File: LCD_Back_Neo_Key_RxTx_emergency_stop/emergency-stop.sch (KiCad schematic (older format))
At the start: 11 parts, among them J6 Screw_Terminal_01x05, K1 FINDER-34.51, K2 FINDER-34.51, K3 FINDER-34.51, Q2 2N2222

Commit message: combine screw terminal
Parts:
- removed J6: Screw_Terminal_01x05, TerminalBlock:TerminalBlock_bornier-5_P5.08mm, symbol Connector:Screw_Terminal_01x05
- removed S1: Emergency Button, symbol LCD_Back_Neo_Key_RxTx_emergency_stop-rescue:Ext_switch
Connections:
- net labels added: ScrewTerm10-EmrgencyRelay12, ScrewTerm11-EmrgencyRelay14, ScrewTerm12-EmrgencyRelay11, ScrewTerm13-EmergencyStopSwitch1, ScrewTerm14-EmergencyStopSwitch2
- wire segments 58 -> 52
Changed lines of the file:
@@
 Wire Wire Line
 	4300 4750 4300 5550
-$Comp
-L Connector:Screw_Terminal_01x05 J6
-U 1 1 5CEE591F
-P 8250 5500
-F 0 "J6" H 8330 5542 50  0000 L CNN
-F 1 "Screw_Terminal_01x05" H 8330 5451 50  0000 L CNN
-F 2 "TerminalBlock:TerminalBlock_bornier-5_P5.08mm" H 8250 5500 50  0001 C CNN
-F 3 "~" H 8250 5500 50  0001 C CNN
-	1    8250 5500
-	1    0    0    -1
-$EndComp
 Wire Wire Line
 	7050 4100 7050 4000
@@
 	7850 4000 7850 5400
 Wire Wire Line
-	7850 5400 8050 5400
-Wire Wire Line
 	6850 4100 6850 3900
 Wire Wire Line
@@
 	7950 3900 7950 5300
 Wire Wire Line
-	7950 5300 8050 5300
-Wire Wire Line
 	6950 4700 6950 5500
-Wire Wire Line
-	6950 5500 8050 5500
-Wire Wire Line
-	8050 5600 6550 5600
 Wire Wire Line
 	6550 5600 6550 5550
 Connection ~ 6550 5550
-Wire Wire Line
-	7950 5700 8050 5700
-$Comp
-L LCD_Back_Neo_Key_RxTx_emergency_stop-rescue:Ext_switch S1
-U 1 1 5CEFD3C6
-P 10050 5200
-F 0 "S1" V 10048 5588 50  0000 L CNN
-F 1 "Emergency Button" V 10139 5588 50  0000 L CNN
-F 2 "" H 9850 5200 50  0001 C CNN
-F 3 "http://www.te.com/commerce/DocumentDelivery/DDEController?Action=srchrtrv&DocNm=108-98001&DocType=SS&DocLang=EN" H 9850 5200 50  0001 C CNN
-	1    10050 5200
-	0    1    1    0
-$EndComp
-Wire Wire Line
-	8250 5600 9700 5600
-Wire Wire Line
-	8250 5700 9450 5700
-Wire Wire Line
-	9450 5700 9450 6100
 $Comp
 L Device:R R?
@@
 	6550 2600 7350 2600
 Connection ~ 6550 2600
-Wire Wire Line
-	10550 6100 10550 5500
-Wire Wire Line
-	10550 5500 10350 5500
-Wire Wire Line
-	9450 6100 10550 6100
 Text GLabel 7800 3000 2    50   Input ~ 0
 Ardu_A6
@@
 Wire Wire Line
 	2000 2950 2500 2950
+Text GLabel 8150 5600 2    50   Input ~ 0
+ScrewTerm13-EmergencyStopSwitch1
+Text GLabel 8150 5700 2    50   Input ~ 0
+ScrewTerm14-EmergencyStopSwitch2
+Text GLabel 8150 5300 2    50   Input ~ 0
+ScrewTerm10-EmrgencyRelay12
+Text GLabel 8150 5400 2    50   Input ~ 0
+ScrewTerm11-EmrgencyRelay14
+Text GLabel 8150 5500 2    50   Input ~ 0
+ScrewTerm12-EmrgencyRelay11
+Wire Wire Line
+	7950 5300 8150 5300
+Wire Wire Line
+	7850 5400 8150 5400
+Wire Wire Line
+	6950 5500 8150 5500
+Wire Wire Line
+	6550 5600 8150 5600
+Wire Wire Line
+	7950 5700 8150 5700
 $EndSCHEMATC

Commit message: update
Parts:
- D? (x2): symbol Diode:1N4004 -> LCD_Back_Neo_Key_RxTx_emergency_stop-rescue:1N4004-Diode
- K1, K2, K3: symbol Relay:FINDER-34.51 -> LCD_Back_Neo_Key_RxTx_emergency_stop-rescue:FINDER-34.51-Relay
- Q2: symbol Transistor_BJT:2N2219 -> LCD_Back_Neo_Key_RxTx_emergency_stop-rescue:2N2219-Transistor_BJT
- R3, R4, R5: symbol Device:R -> LCD_Back_Neo_Key_RxTx_emergency_stop-rescue:R-Device
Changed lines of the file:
@@
 $EndDescr
 $Comp
-L Relay:FINDER-34.51 K3
+L LCD_Back_Neo_Key_RxTx_emergency_stop-rescue:FINDER-34.51-Relay K3
 U 1 1 5CED36F4
 P 6750 4400
@@
 $EndComp
 $Comp
-L Relay:FINDER-34.51 K2
+L LCD_Back_Neo_Key_RxTx_emergency_stop-rescue:FINDER-34.51-Relay K2
 U 1 1 5CED5653
 P 4500 4450
@@
 	4700 4950 4700 4750
 $Comp
-L Relay:FINDER-34.51 K1
+L LCD_Back_Neo_Key_RxTx_emergency_stop-rescue:FINDER-34.51-Relay K1
 U 1 1 5CED8027
 P 2700 3700
@@
 	4300 4000 4300 4150
 $Comp
-L Transistor_BJT:2N2219 Q2
+L LCD_Back_Neo_Key_RxTx_emergency_stop-rescue:2N2219-Transistor_BJT Q2
 U 1 1 5CED966B
 P 2350 4750
@@
 Connection ~ 6550 5550
 $Comp
-L Device:R R?
+L LCD_Back_Neo_Key_RxTx_emergency_stop-rescue:R-Device R?
 U 1 1 5CF0A2FB
 P 1800 4750
@@
 	1400 4750 1650 4750
 $Comp
-L Device:R R?
+L LCD_Back_Neo_Key_RxTx_emergency_stop-rescue:R-Device R?
 U 1 1 5CF0BD5A
 P 7350 2750
@@
 $EndComp
 $Comp
-L Device:R R?
+L LCD_Back_Neo_Key_RxTx_emergency_stop-rescue:R-Device R?
 U 1 1 5CF0C775
 P 7350 3200
@@
 Connection ~ 7350 3000
 $Comp
-L Diode:1N4004 D?
+L LCD_Back_Neo_Key_RxTx_emergency_stop-rescue:1N4004-Diode D?
 U 1 1 5CEE427E
 P 5950 4400
@@
 $EndComp
 $Comp
-L Diode:1N4004 D?
+L LCD_Back_Neo_Key_RxTx_emergency_stop-rescue:1N4004-Diode D?
 U 1 1 5CEE5957
 P 2000 3700

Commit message: place screwterminal on PCB
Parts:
- added JP1, JP2: Jumper_lon-jumper_lon, Jumper:SolderJumper-2_P1.3mm_Open_Pad1.0x1.5mm, symbol ArduMicro:Jumper_lon-jumper_lon
- added K4: FINDER-34.51, Relay_THT:Relay_SPDT_Finder_34.51_Vertical, symbol LCD_Back_Neo_Key_RxTx_emergency_stop-rescue:FINDER-34.51-Relay
- gave numbers to parts that had none: 2
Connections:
- net GND: now also JP2.2
- net VCC-24V: now also K4.A1
- net ScrewTerm10-EmrgencyRelay12 renamed ScrewTerm8-EmrgencyRelay12
- net ScrewTerm11-EmrgencyRelay14 renamed ScrewTerm9-EmrgencyRelay14
- net ScrewTerm12-EmrgencyRelay11 renamed ScrewTerm10-EmrgencyRelay11
- net ScrewTerm13-EmergencyStopSwitch1: no longer names the net of D2.2 (A), K2.A2, K3.A2
- net ScrewTerm13-EmergencyStopSwitch1: now also JP1.1, K4.12
- new net ScrewTerm11-EmergencyStopSwitch1: JP1.2, JP2.1, K4.11
- new net ScrewTerm13-EmergencyStopSwitch3: K4.A2
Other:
- moved on the sheet: D1, D2, K1, K2, K3, Q2, R3, R4, R5

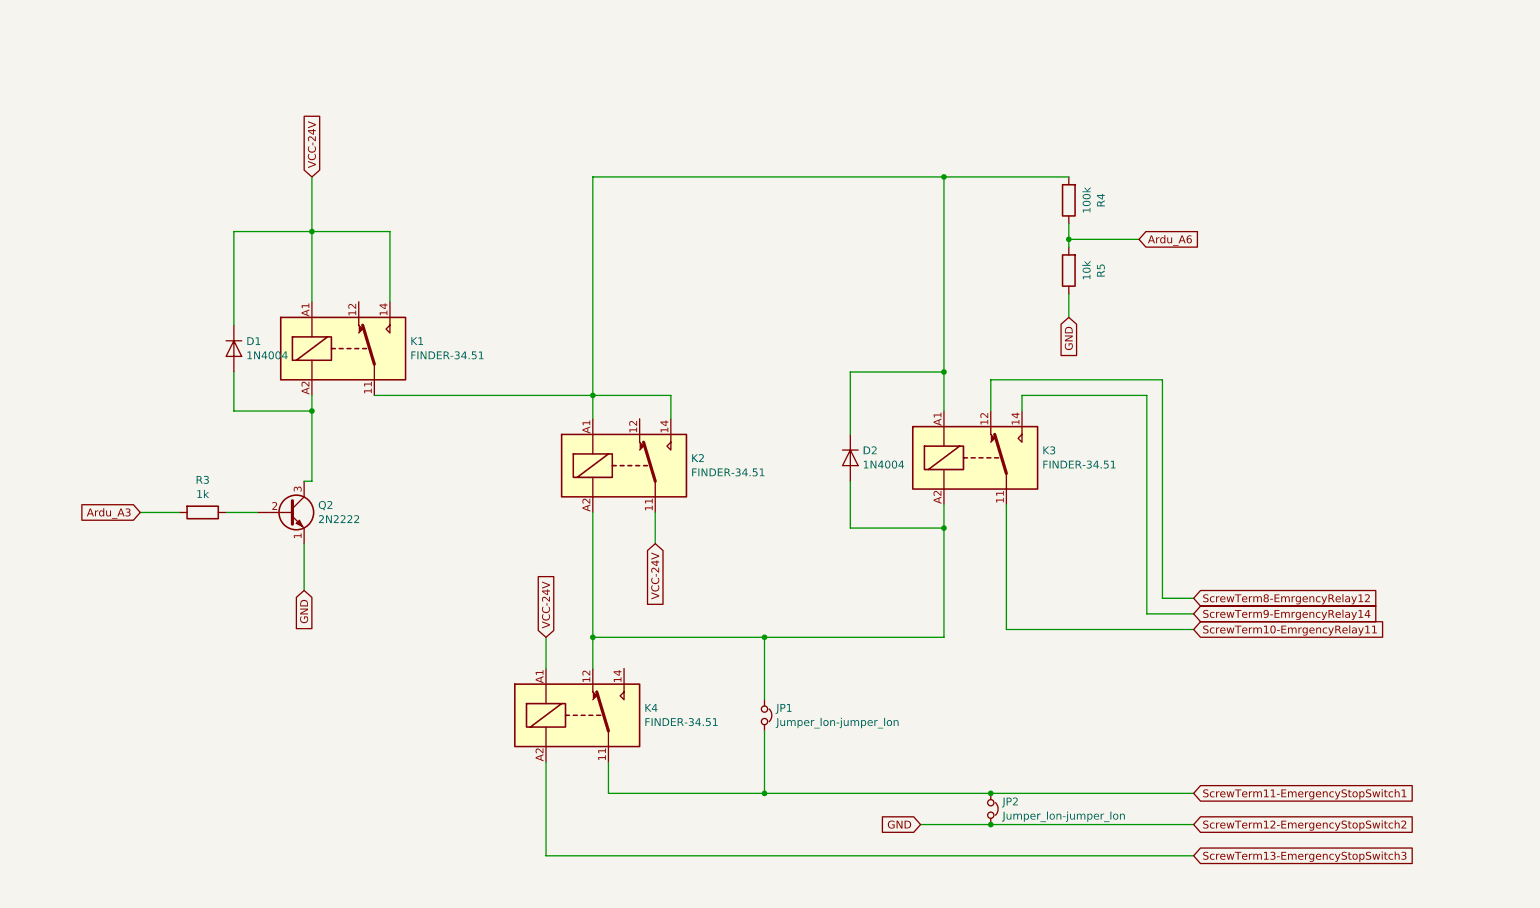
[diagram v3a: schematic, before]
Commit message: remove all through-connection. Manufacturer can't handle
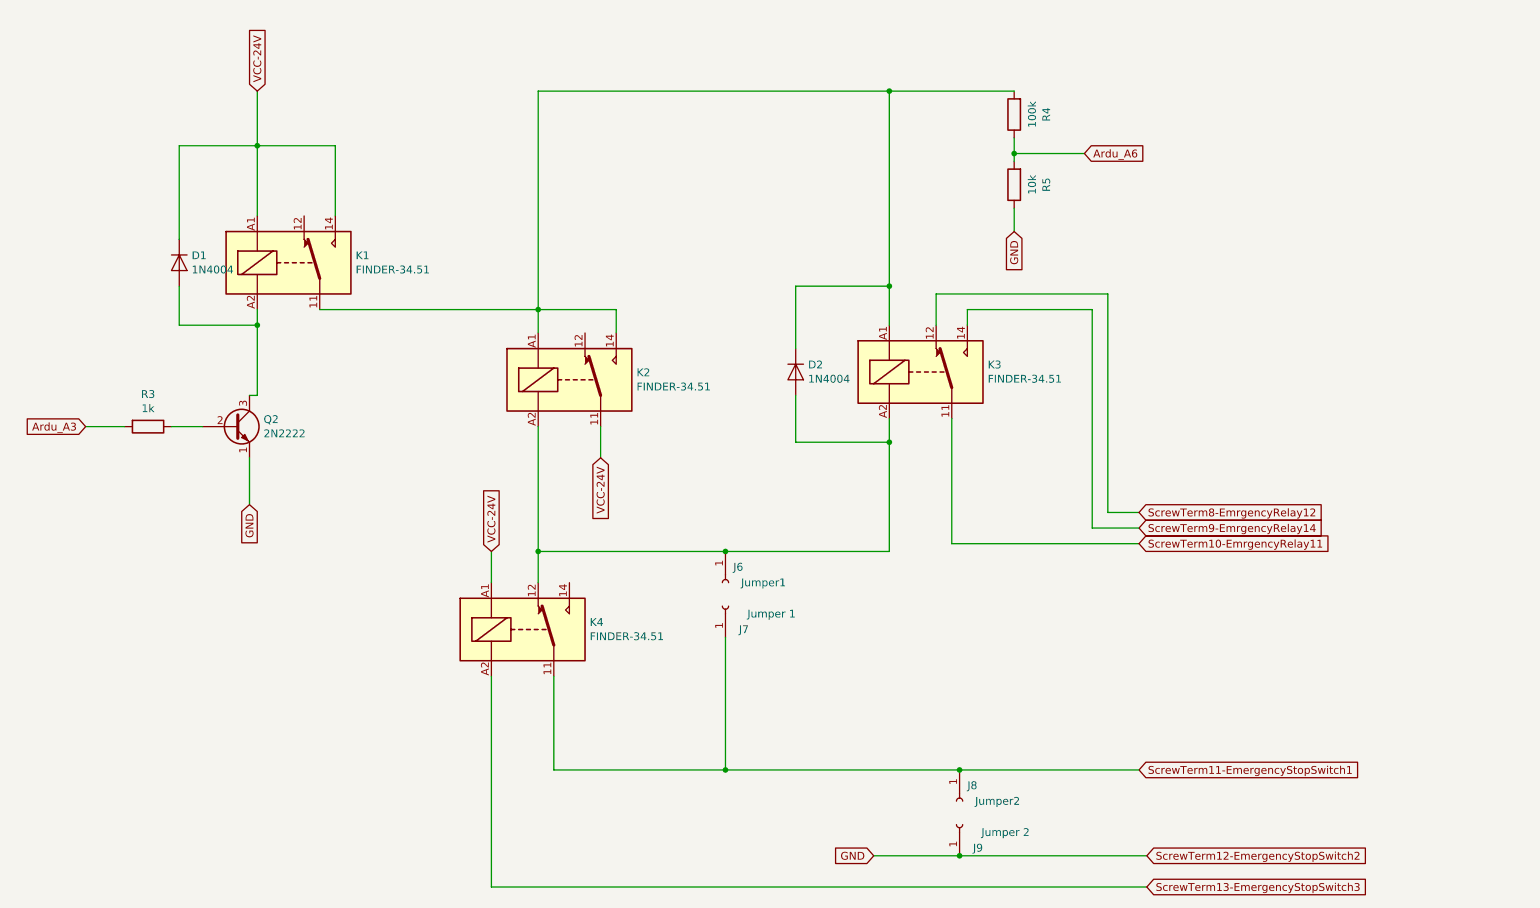
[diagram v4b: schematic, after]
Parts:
- removed JP1, JP2: Jumper_lon-jumper_lon, Jumper:SolderJumper-2_P1.3mm_Open_Pad1.0x1.5mm, symbol ArduMicro:Jumper_lon-jumper_lon
- added J6: Jumper1, Connector_Pin:Pin_D0.7mm_L6.5mm_W1.8mm_FlatFork, symbol LCD_Back_Neo_Key_RxTx_emergency_stop-rescue:Conn_01x01_Female-Connector
- added J7: Jumper 1, Connector_Pin:Pin_D0.7mm_L6.5mm_W1.8mm_FlatFork, symbol LCD_Back_Neo_Key_RxTx_emergency_stop-rescue:Conn_01x01_Female-Connector
- added J8: Jumper2, Connector_Pin:Pin_D0.7mm_L6.5mm_W1.8mm_FlatFork, symbol LCD_Back_Neo_Key_RxTx_emergency_stop-rescue:Conn_01x01_Female-Connector
- added J9: Jumper 2, Connector_Pin:Pin_D0.7mm_L6.5mm_W1.8mm_FlatFork, symbol LCD_Back_Neo_Key_RxTx_emergency_stop-rescue:Conn_01x01_Female-Connector
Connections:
- net GND: now also J9.1 (Pin_1)
- net ScrewTerm11-EmergencyStopSwitch1: now also J7.1 (Pin_1), J8.1 (Pin_1)
- net at D2.2 (A), K2.A2, K3.A2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: now also J6.1 (Pin_1)
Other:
- moved on the sheet: D1, D2, K1, K2, K3, K4, Q2, R3, R4, R5
